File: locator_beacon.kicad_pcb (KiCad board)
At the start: 2 copper layers, 50.9 x 20.8 mm, 35 parts, among them J1 Conn_01x02, J2 Conn_01x02, Q1 DMN6140, Q2 DMN6140, Q3 DMN6140, Q4 DMN6140, U1 MC34063AD, U13 Pico, U3 MIC4606

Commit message: Stuff
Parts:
- moved C11 0.63 mm to (137.5, 73.4)
- moved C2 0.25 mm to (127.3, 74.4)

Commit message: changes
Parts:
- removed REF**: KiCad-Logo_5mm_Copper, Symbol:KiCad-Logo_5mm_Copper
- removed U1: MC34063AD, Package_SO:SOIC-8_3.9x4.9mm_P1.27mm
- added C12: C, Capacitor_SMD:CP_Elec_6.3x7.7, F.Cu at (136.1, 72.6)
- added C13: 10u, Capacitor_SMD:C_0603_1608Metric, F.Cu at (141.2, 81.7)
- added C16: 10u, Capacitor_SMD:C_0603_1608Metric, F.Cu at (141.2, 83.2)
- added C18: 10u, Capacitor_SMD:C_0603_1608Metric, F.Cu at (141.2, 80.1)
- added C19: 10u, Capacitor_SMD:C_0603_1608Metric, F.Cu at (141.2, 78.6)
- added C20: 10u, Capacitor_SMD:C_0603_1608Metric, F.Cu at (141.4, 71.4)
- added C6: 10u, Capacitor_SMD:C_0603_1608Metric, F.Cu at (141.2, 84.7)
- added C8: 10u, Capacitor_SMD:C_0603_1608Metric, F.Cu at (141.4, 69.8)
- added C9: 10u, Capacitor_SMD:C_0603_1608Metric, F.Cu at (141.4, 72.9)
- added D1: DSS16U, Diode_SMD:D_SOD-123, F.Cu at (126.4, 84.6)
- added J3: Conn_01x01, Connector_PinHeader_2.54mm:PinHeader_1x01_P2.54mm_Vertical, F.Cu at (155.8, 84.2)
- added J4: OSHW logo, Symbol:OSHW-Logo_5.7x6mm_Copper, F.Cu at (165.2, 70.9)
- added J6: Conn_01x01, Connector_PinHeader_2.54mm:PinHeader_1x01_P2.54mm_Vertical, F.Cu at (121.7, 69.6)
- added J7: Conn_01x02, Connector_PinHeader_2.54mm:PinHeader_1x02_P2.54mm_Vertical, F.Cu at (159.8, 69.6)
- added U2: MIC2288, Package_SO:TSOP-5_1.65x3.05mm_P0.95mm, F.Cu at (123.1, 75.6)
- C2: value 1.5n -> C; footprint Capacitor_SMD:C_0603_1608Metric -> Capacitor_SMD:CP_Elec_6.3x7.7
- J1, J2: footprint Connector_PinHeader_2.54mm:PinHeader_1x02_P2.54mm_Horizontal -> custom:SAMTEC_TSM-102-01-L-SH
- L1: footprint Inductor_SMD:L_Taiyo-Yuden_MD-4040 -> custom:IND_357100_WRE
- U13: footprint custom:rp_pico -> custom:RPi_pico
- moved C2 11.7 mm to (136.1, 82.0)
- moved TP1 9.00 mm to (131.7, 85.6)
- moved C14 7.98 mm to (141.4, 74.4), turned to 0 degrees
- moved R5 6.94 mm to (150.6, 82.0), turned to 90 degrees
- moved R1 6.87 mm to (160.0, 72.5), turned to 90 degrees
- moved C17 6.86 mm to (160.0, 75.8), turned to 90 degrees
- moved R7 6.78 mm to (150.6, 73.2), turned to 90 degrees
- moved TP7 6.08 mm to (151.1, 70.6)
- moved R9 5.85 mm to (149.0, 73.9), turned to 90 degrees
- moved TP6 5.64 mm to (148.8, 71.4)
- moved R3 5.62 mm to (149.1, 80.6), turned to 90 degrees
- moved TP2 5.51 mm to (150.6, 84.6)
- moved L1 5.49 mm to (129.5, 76.5), turned to 0 degrees
- moved Q4 5.05 mm to (144.9, 74.8), turned to 90 degrees
- moved TP4 4.99 mm to (148.6, 83.2)
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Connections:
- C2 pad 1: Net-(U1-TC) -> Vdrive
- TP2 pad 1: /amplifier/L_HI -> Net-(Q1-G)
- TP4 pad 1: /amplifier/L_LO -> Net-(Q2-G)
- TP6 pad 1: /amplifier/R_LO -> Net-(Q4-G)
- TP7 pad 1: /amplifier/R_HI -> Net-(Q3-G)
- U13 pad 2: unconnected-(U13-GPIO1-Pad2) -> /power/EN
- U13 pad 25: unconnected-(U13-GPIO19-Pad25) -> /amplifier/EN
- U13 pad 29: /amplifier/EN -> unconnected-(U13-GPIO22-Pad29)
- U13 pad 39: +BATT -> Net-(D1-K)
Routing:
- net Vdrive: track 31.2 -> 72.7 mm
- net GND: track 63.4 -> 83.9 mm, vias 3 -> 4
- net /amplifier/OUT_B: track 39.4 -> 29.7 mm, vias 2 -> 3
- net Net-(Q4-G): track 1.51 -> 10.1 mm, vias 0 -> 2
- net +BATT: track 23.8 -> 15.9 mm
- net /amplifier/SIG_IN: track 10.5 -> 2.58 mm
- net /power/EN: track 0.00 -> 7.78 mm
- net Net-(U2-FB): track 13.5 -> 5.89 mm
- net /amplifier/OUT_A: track 35.1 -> 28.9 mm, vias 2 -> 3
- net Net-(Q1-G): track 1.74 -> 7.49 mm
- net Net-(Q3-G): track 3.62 -> 9.13 mm, vias 0 -> 2
- net Net-(D3-A): track 7.48 -> 12.4 mm
- net /amplifier/~{SIG_IN}: track 7.66 -> 2.90 mm
- net Net-(Q2-G): track 1.78 -> 6.00 mm
- net Net-(D1-K): track 0.00 -> 4.15 mm, vias 0 -> 1
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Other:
- board size 50.9 x 20.8 mm -> 51 x 22.5 mm
- board text added: "OUT"
- board text added: "github.com/one-ping-only"
- board text added: "locator v2.1"
- board text removed: "ONE PING ONLY"
- board text removed: "TX V2"

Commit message: Shrunkified
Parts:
- removed C2: C, Capacitor_SMD:CP_Elec_6.3x7.7
- removed C6, C8: 10u, Capacitor_SMD:C_0603_1608Metric
- added J5: Conn_01x02, Connector_PinHeader_2.54mm:PinHeader_1x02_P2.54mm_Vertical, F.Cu at (121.7, 87.3)
- moved TP1 14.2 mm to (136.1, 72.1)
- moved C12 6.10 mm to (136.3, 78.7)
- moved L1 4.07 mm to (129.7, 80.5)
- moved J3 3.44 mm to (157.2, 87.3), turned to 0 degrees
- moved D3 3.30 mm to (132.5, 84.3), turned to 180 degrees
- moved RV1 3.30 mm to (129.7, 74.4), turned to 180 degrees
- moved J4 0.46 mm to (165.0, 71.2)
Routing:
- net Vdrive: track 72.7 -> 57.1 mm
- net GND: track 83.9 -> 71.1 mm, vias 4 -> 3
- net Net-(D3-A): track 12.4 -> 17.4 mm
- net Net-(U2-FB): track 5.89 -> 9.17 mm
- net +BATT: track 15.9 -> 14.2 mm
- net /amplifier/EN: track 10.1 -> 8.79 mm, vias 1 -> 0
- added copper zone on F.Cu, net Vdrive
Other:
- board size 51 x 22.5 mm -> 51 x 21.3 mm

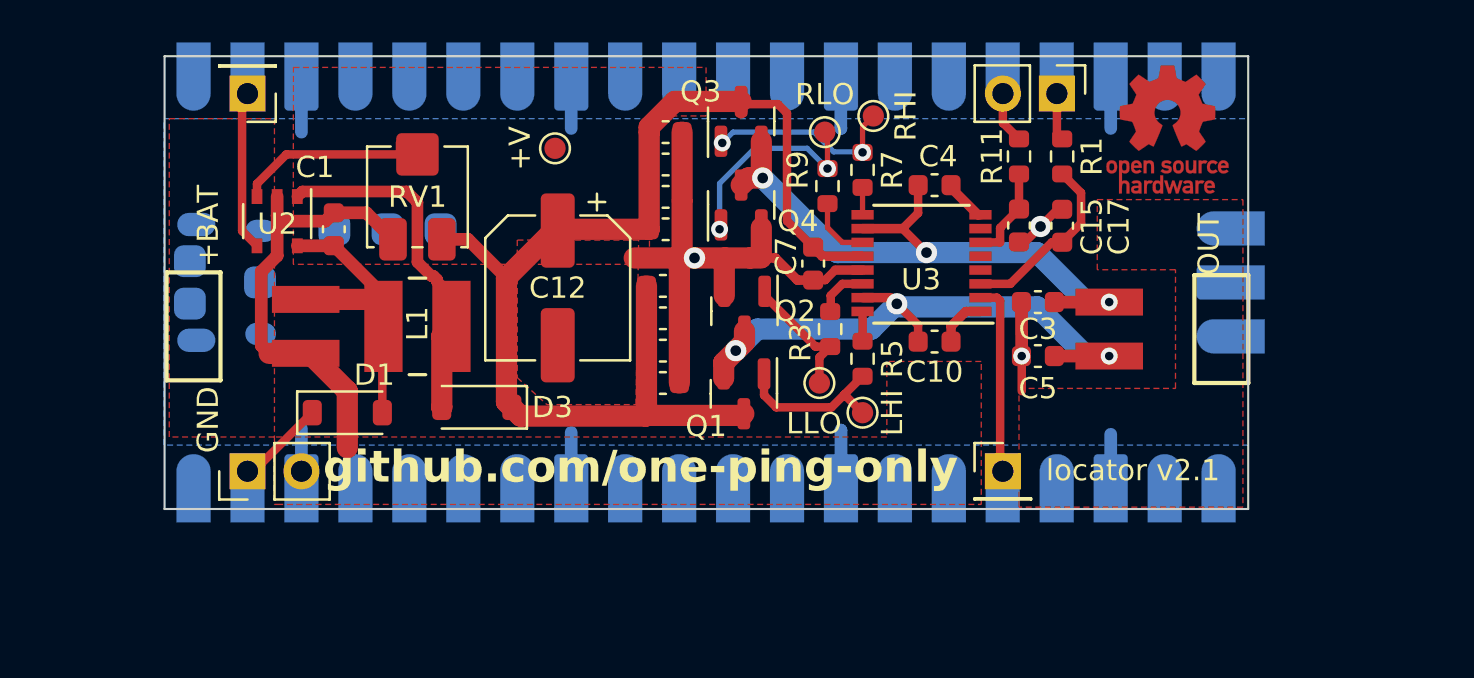
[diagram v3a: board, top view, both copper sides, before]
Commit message: Separate +12 and boost
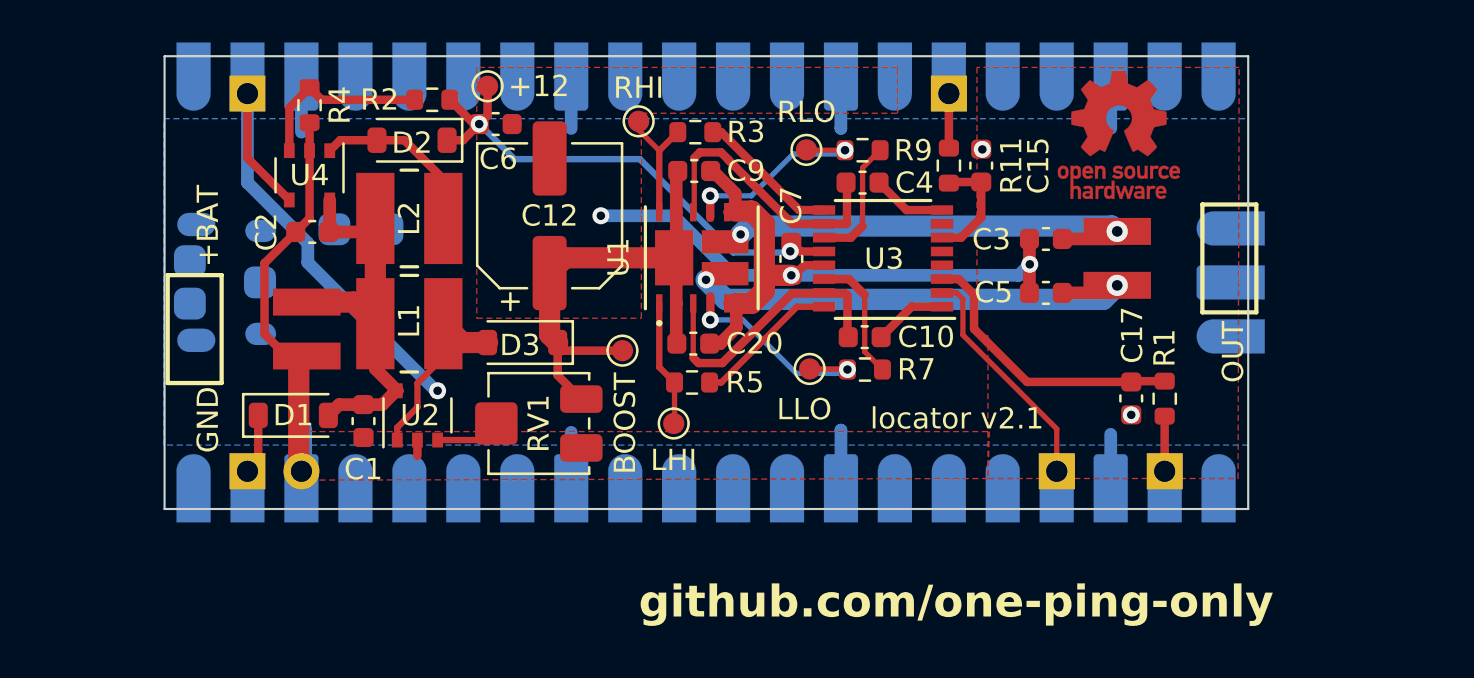
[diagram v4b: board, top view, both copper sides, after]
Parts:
- removed C11, C13, C14, C16, C18, C19: 10u, Capacitor_SMD:C_0603_1608Metric
- removed Q1, Q2, Q3, Q4: DMN6140, Package_TO_SOT_SMD:SOT-23
- added +12: +12, TestPoint:TestPoint_Pad_D1.0mm, F.Cu at (133.0, 69.2)
- added C2: C, Capacitor_SMD:C_0603_1608Metric, F.Cu at (124.7, 76.1)
- added C6: 10u, Capacitor_SMD:C_0603_1608Metric, F.Cu at (133.3, 71.0)
- added D2: DSS16U, Diode_SMD:D_SOD-123, F.Cu at (129.4, 71.8)
- added J8: Conn_01x01, Connector_PinHeader_2.54mm:PinHeader_1x01_P2.54mm_Vertical, F.Cu at (154.7, 69.6)
- added L2: 10u, custom:IND_357100_WRE, F.Cu at (129.3, 75.4)
- added R2: 42.3k, Resistor_SMD:R_0603_1608Metric, F.Cu at (130.4, 69.8)
- added R4: 5k, Resistor_SMD:R_0603_1608Metric, F.Cu at (124.6, 70.1)
- added U1: DMHT6016LFJ-13, custom:V-DFN5045-12_DIO, F.Cu at (143.1, 77.3)
- added U4: MIC2288, Package_SO:TSOP-5_1.65x3.05mm_P0.95mm, F.Cu at (124.6, 73.4)
- J7: value Conn_01x02 -> Conn_01x01; footprint Connector_PinHeader_2.54mm:PinHeader_1x02_P2.54mm_Vertical -> Connector_PinHeader_2.54mm:PinHeader_1x01_P2.54mm_Vertical
- TP1: value +V -> BOOST
- moved J7 18.5 mm to (164.8, 87.3), turned to 0 degrees
- moved R1 12.4 mm to (164.8, 83.9), turned to -90 degrees
- moved RV1 12.1 mm to (135.4, 85.1), turned to -90 degrees
- moved U2 11.3 mm to (129.7, 84.7), turned to 90 degrees
- moved R3 11.2 mm to (142.7, 71.4), turned to 0 degrees
- moved TP7 11.1 mm to (140.1, 70.9), turned to 180 degrees
- moved C20 10.0 mm to (142.7, 81.3)
- moved TP1 10.0 mm to (139.3, 81.7)
- moved R7 9.40 mm to (150.7, 82.5), turned to 0 degrees
- moved C1 9.14 mm to (127.1, 85.0), turned to -90 degrees
- moved TP2 8.90 mm to (141.7, 85.1)
- moved C17 8.75 mm to (163.3, 83.9), turned to -90 degrees
- moved R5 8.10 mm to (142.6, 83.2), turned to 0 degrees
- moved D3 3.74 mm to (134.6, 81.3)
- moved C12 3.42 mm to (135.9, 75.3), turned to 90 degrees
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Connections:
- C12 pad 1: Vdrive -> V_{boost}
- C20 pad 1: Vdrive -> V_{boost}
- C7 pad 1: Vdrive -> +12V
- C9 pad 1: Vdrive -> V_{boost}
- D3 pad 1: Vdrive -> V_{boost}
- R3 pad 1: Net-(Q2-G) -> /amplifier/R_HI
- R3 pad 2: /amplifier/L_LO -> Net-(U3-AHO)
- R5 pad 1: Net-(Q1-G) -> /amplifier/L_HI
- R5 pad 2: /amplifier/L_HI -> Net-(U3-BHO)
- R7 pad 1: /amplifier/R_HI -> /amplifier/L_LO
- R7 pad 2: Net-(Q3-G) -> Net-(U3-BLO)
- R9 pad 2: Net-(Q4-G) -> Net-(U3-ALO)
- RV1 pad 1: Vdrive -> V_{boost}
- TP1 pad 1: Vdrive -> V_{boost}
- TP2 pad 1: Net-(Q1-G) -> /amplifier/L_HI
- TP4 pad 1: Net-(Q2-G) -> /amplifier/L_LO
- TP6 pad 1: Net-(Q4-G) -> /amplifier/R_LO
- TP7 pad 1: Net-(Q3-G) -> /amplifier/R_HI
- U13 pad 15: unconnected-(U13-GPIO11-Pad15) -> /amplifier/~{SIG_IN}
- U13 pad 16: /amplifier/~{SIG_IN} -> unconnected-(U13-GPIO12-Pad16)
- U13 pad 17: /amplifier/SIG_IN -> unconnected-(U13-GPIO13-Pad17)
- U13 pad 22: unconnected-(U13-GPIO17-Pad22) -> /amplifier/SIG_IN
- U13 pad 24: unconnected-(U13-GPIO18-Pad24) -> /amplifier/EN
- U13 pad 25: /amplifier/EN -> unconnected-(U13-GPIO19-Pad25)
- U3 pad 11: /amplifier/R_LO -> Net-(U3-ALO)
- U3 pad 12: Vdrive -> +12V
- U3 pad 14: /amplifier/L_LO -> Net-(U3-BLO)
- U3 pad 16: /amplifier/L_HI -> Net-(U3-BHO)
- U3 pad 9: /amplifier/R_HI -> Net-(U3-AHO)
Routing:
- net Vdrive: track 57.1 -> 0.00 mm
- net +12V: track 0.00 -> 25.0 mm, vias 0 -> 2
- net V_{boost}: track 0.00 -> 23.8 mm
- net /power/EN: track 7.78 -> 23.6 mm, vias 0 -> 1
- net Net-(Q4-G): track 10.1 -> 0.00 mm, vias 2 -> 0
- net Net-(Q3-G): track 9.13 -> 0.00 mm, vias 2 -> 0
- net Net-(D3-A): track 17.4 -> 8.83 mm
- net Net-(U4-FB): track 0.00 -> 8.55 mm
- net Net-(D2-A): track 0.00 -> 8.16 mm
- net /amplifier/L_LO: track 2.49 -> 10.5 mm, vias 0 -> 2
- net Net-(Q1-G): track 7.49 -> 0.00 mm
- net Net-(U3-AHO): track 0.00 -> 7.30 mm
- net /amplifier/OUT_A: track 28.9 -> 36.0 mm, vias 3 -> 2
- net /amplifier/R_LO: track 3.07 -> 10.1 mm, vias 0 -> 2
- net Net-(U3-BHO): track 0.00 -> 6.48 mm
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- removed copper zone on F.Cu, net Vdrive
